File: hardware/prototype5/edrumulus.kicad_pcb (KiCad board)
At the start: 2 copper layers, 65 x 56.5 mm, 79 parts, among them J1 Trigger Connector, J2 Raspberry Pi GPIO pins, U1 ESP32-WROOM-32U, U2 AMS1117-3.3, U3 MCP1754S-3302xMB

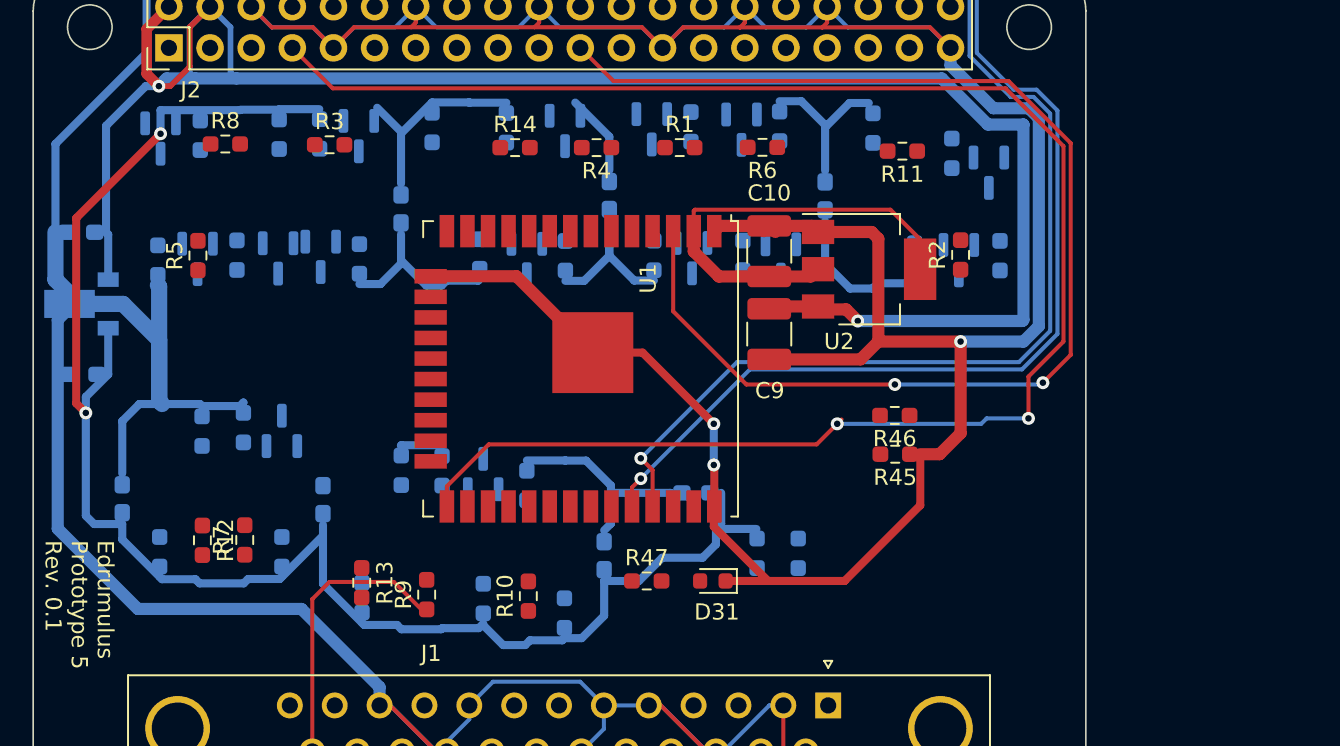
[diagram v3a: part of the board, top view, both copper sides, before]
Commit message: added the caps on the lower bias resistor for prototype 5
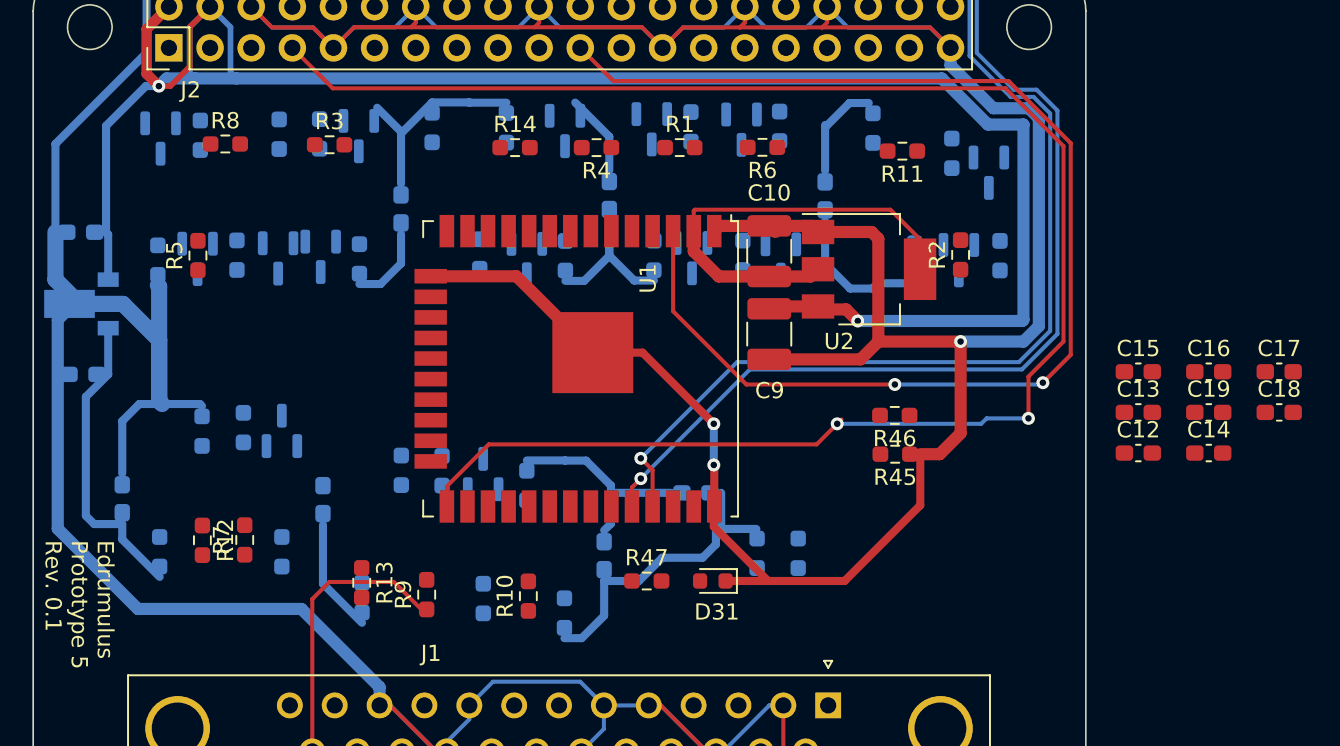
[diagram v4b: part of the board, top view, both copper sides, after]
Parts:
- added C12: 2n2, Capacitor_SMD:C_0603_1608Metric_Pad1.08x0.95mm_HandSolder, F.Cu at (174.8, 103.4)
- added C13: 2n2, Capacitor_SMD:C_0603_1608Metric_Pad1.08x0.95mm_HandSolder, F.Cu at (174.8, 100.9)
- added C14: 2n2, Capacitor_SMD:C_0603_1608Metric_Pad1.08x0.95mm_HandSolder, F.Cu at (179.2, 103.4)
- added C15: 2n2, Capacitor_SMD:C_0603_1608Metric_Pad1.08x0.95mm_HandSolder, F.Cu at (174.8, 98.4)
- added C16: 2n2, Capacitor_SMD:C_0603_1608Metric_Pad1.08x0.95mm_HandSolder, F.Cu at (179.2, 98.4)
- added C17: 2n2, Capacitor_SMD:C_0603_1608Metric_Pad1.08x0.95mm_HandSolder, F.Cu at (183.5, 98.4)
- added C18: 2n2, Capacitor_SMD:C_0603_1608Metric_Pad1.08x0.95mm_HandSolder, F.Cu at (183.5, 100.9)
- added C19: 2n2, Capacitor_SMD:C_0603_1608Metric_Pad1.08x0.95mm_HandSolder, F.Cu at (179.2, 100.9)
- C1, C2, C3, C4, C5, C6, C7: value 100 nF -> 100n
- C10, C9: value 22 µF -> 22µ
- C11, C8: value 1 µF -> 1µ
- R1, R12, R2, R3, R4, R5, R6, R7, R8, R9: value 100 kOhm -> 100k
- R10, R11, R13, R14: value 100 kOhm -> 22k
- R15, R16, R17, R18, R19, R20, R21, R22, R23, R24, R25, R26, R27, R28, R30, R32, R34, R38, R39, R40, R41, R42, R43, R44: value 22 kOhm -> 22k
- R29, R31, R35, R36: value 22 kOhm -> 100k
- R33, R37, R45, R46: value 10 kOhm -> 10k
- R47: value 470 Ohm -> 470
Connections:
- D12 pad 3: Net-(D12-Pad3) -> Net-(C17-Pad1)
- D13 pad 3: Net-(D13-Pad3) -> Net-(C18-Pad1)
- D3 pad 3: GPIO26 -> GPIO14
- D5 pad 3: GPIO14 -> GPIO26
- R10 pad 1: TOM1-RING -> GPIO14
- R10 pad 2: GPIO4 -> CRASH1-SLEEVE
- R11 pad 1: TOM1-TIP -> Net-(D4-Pad3)
- R11 pad 2: GPIO39 -> CRASH1-SLEEVE
- R13 pad 1: GPIO15 -> GPIO26
- R13 pad 2: TOM3-TIP -> CRASH1-SLEEVE
- R14 pad 1: GPIO33 -> Net-(D6-Pad3)
- R14 pad 2: KICK-TIP -> CRASH1-SLEEVE
- R17 pad 1: GPIO26 -> GPIO13
- R18 pad 1: Net-(D4-Pad3) -> Net-(D8-Pad3)
- R19 pad 1: GPIO14 -> Net-(D9-Pad3)
- R20 pad 1: Net-(D6-Pad3) -> 3V3
- R20 pad 2: CRASH1-SLEEVE -> GPIO14
- R21 pad 1: GPIO13 -> 3V3
- R21 pad 2: CRASH1-SLEEVE -> Net-(D4-Pad3)
- R22 pad 1: Net-(D8-Pad3) -> 3V3
- R22 pad 2: CRASH1-SLEEVE -> GPIO26
- R23 pad 1: Net-(D9-Pad3) -> 3V3
- R23 pad 2: CRASH1-SLEEVE -> Net-(D6-Pad3)
- R26 pad 2: GPIO26 -> GPIO13
- R27 pad 2: Net-(D4-Pad3) -> Net-(D8-Pad3)
- R28 pad 2: GPIO14 -> Net-(D9-Pad3)
- R29 pad 1: 3V3 -> GPIO15
- R29 pad 2: Net-(D6-Pad3) -> TOM3-TIP
- R3 pad 1: HI-HAT-RING -> CRASH1-RING
- R3 pad 2: GPIO26 -> GPIO14
- R30 pad 1: 3V3 -> Net-(C17-Pad1)
- R30 pad 2: GPIO13 -> CRASH1-SLEEVE
- R31 pad 1: 3V3 -> GPIO33
- R31 pad 2: Net-(D8-Pad3) -> KICK-TIP
- R32 pad 1: 3V3 -> Net-(C18-Pad1)
- R32 pad 2: Net-(D9-Pad3) -> CRASH1-SLEEVE
- R35 pad 1: Net-(D12-Pad3) -> TOM1-RING
- R35 pad 2: CRASH1-SLEEVE -> GPIO4
- R36 pad 1: Net-(D13-Pad3) -> TOM1-TIP
- R36 pad 2: CRASH1-SLEEVE -> GPIO39
- R39 pad 2: Net-(D12-Pad3) -> Net-(C17-Pad1)
- R4 pad 1: HI-HAT-TIP -> CRASH1-TIP
- R4 pad 2: GPIO32 -> GPIO34
- R40 pad 2: Net-(D13-Pad3) -> Net-(C18-Pad1)
- R5 pad 1: CRASH1-RING -> HI-HAT-RING
- R5 pad 2: GPIO14 -> GPIO26
- R6 pad 1: CRASH1-TIP -> HI-HAT-TIP
- R6 pad 2: GPIO34 -> GPIO32
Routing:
- net 3V3: track 128.3 -> 68.4 mm, vias 2 -> 0
- net CRASH1-SLEEVE: track 422.9 -> 412.0 mm

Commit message: delivery jstma for prototype 5 on 8/24/2022
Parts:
- added C20: 2n2, Capacitor_SMD:C_0603_1608Metric_Pad1.08x0.95mm_HandSolder, B.Cu at (127.8, 99.2)
- added C21: 2n2, Capacitor_SMD:C_0603_1608Metric_Pad1.08x0.95mm_HandSolder, B.Cu at (134.2, 99.2)
- added C22: 2n2, Capacitor_SMD:C_0603_1608Metric_Pad1.08x0.95mm_HandSolder, B.Cu at (131.0, 99.2)
- added C23: 2n2, Capacitor_SMD:C_0603_1608Metric_Pad1.08x0.95mm_HandSolder, B.Cu at (140.6, 99.2)
- added C24: 2n2, Capacitor_SMD:C_0603_1608Metric_Pad1.08x0.95mm_HandSolder, B.Cu at (143.6, 84.4)
- added C25: 2n2, Capacitor_SMD:C_0603_1608Metric_Pad1.08x0.95mm_HandSolder, B.Cu at (129.4, 99.2)
- C1, C11, C2, C3, C4, C5, C6, C7, C8, D10, R20, R21, R22, R23, R24, R25, R26, R27, R28, R31, R33, R37, R38, R39, R40, R43, R44, U3: moved to F.Cu
- C12, C13, C14, C15, C16, C17, C18, C19, R10, R11, R12, R13, R14, R45, R46, R7, R8, R9: moved to B.Cu
- moved D14 56.7 mm to (151.6, 126.8), turned to 90 degrees
- moved C18 47.7 mm to (135.8, 99.2), turned to 90 degrees
- moved R31 46.2 mm to (156.0, 114.8)
- moved D11 45.2 mm to (146.0, 126.8), turned to 90 degrees
- moved D12 44.4 mm to (138.0, 126.8), turned to 90 degrees
- moved R29 44.1 mm to (136.4, 124.2), turned to 90 degrees
- moved D15 43.9 mm to (157.2, 126.8), turned to 90 degrees
- moved D31 43.8 mm to (111.2, 88.4)
- moved C9 42.5 mm to (111.6, 83.0), turned to 90 degrees
- moved C13 42.2 mm to (132.6, 99.2), turned to 90 degrees
- moved C19 41.8 mm to (137.4, 99.2), turned to 90 degrees
- moved C17 41.8 mm to (143.6, 86.0), turned to 180 degrees
- moved U2 41.8 mm to (117.0, 85.0), turned to -90 degrees
- moved R8 41.3 mm to (126.6, 124.8), turned to -90 degrees
- moved R47 41.2 mm to (111.2, 87.0)
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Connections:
- net CRASH1-SLEEVE renamed GND
- C12 pad 1: GPIO14 -> GPIO36
- C16 pad 1: Net-(R34-Pad1) -> GPIO12
- C17 pad 1: Net-(C17-Pad1) -> GPIO15
- C18 pad 1: Net-(C18-Pad1) -> GPIO33
- C19 pad 1: GPIO4 -> GPIO25
- D10 pad 3: Net-(D10-Pad3) -> HI-HAT-CONTROL-TIP
- D11 pad 3: Net-(R34-Pad1) -> GPIO12
- D12 pad 3: Net-(C17-Pad1) -> GPIO15
- D13 pad 3: Net-(C18-Pad1) -> GPIO33
- D14 pad 3: GPIO4 -> GPIO25
- D15 pad 3: Net-(D15-Pad3) -> GPIO39
- D2 pad 3: Net-(R16-Pad1) -> GPIO14
- D3 pad 3: GPIO14 -> GPIO36
- D4 pad 3: Net-(D4-Pad3) -> GPIO34
- D6 pad 3: Net-(D6-Pad3) -> GPIO32
- D8 pad 3: Net-(D8-Pad3) -> GPIO27
- D9 pad 3: Net-(D9-Pad3) -> GPIO2
- R10 pad 1: GPIO14 -> GPIO36
- R11 pad 1: Net-(D4-Pad3) -> GPIO34
- R14 pad 1: Net-(D6-Pad3) -> GPIO32
- R16 pad 1: Net-(R16-Pad1) -> GPIO14
- R18 pad 1: Net-(D8-Pad3) -> GPIO27
- R19 pad 1: Net-(D9-Pad3) -> GPIO2
- R2 pad 2: GPIO36 -> GPIO14
- R20 pad 2: GPIO14 -> GPIO36
- R21 pad 2: Net-(D4-Pad3) -> GPIO34
- R23 pad 2: Net-(D6-Pad3) -> GPIO32
- R25 pad 2: Net-(R16-Pad1) -> GPIO14
- R27 pad 2: Net-(D8-Pad3) -> GPIO27
- R28 pad 2: Net-(D9-Pad3) -> GPIO2
- R3 pad 2: GPIO14 -> GPIO36
- R30 pad 1: Net-(C17-Pad1) -> GPIO15
- R32 pad 1: Net-(C18-Pad1) -> GPIO33
- R33 pad 1: GPIO25 -> GPIO4
- R34 pad 1: Net-(R34-Pad1) -> GPIO12
- R35 pad 2: GPIO4 -> GPIO25
- R37 pad 2: Net-(D10-Pad3) -> HI-HAT-CONTROL-TIP
- R38 pad 2: Net-(R34-Pad1) -> GPIO12
- R39 pad 2: Net-(C17-Pad1) -> GPIO15
- R40 pad 2: Net-(C18-Pad1) -> GPIO33
- R41 pad 1: GPIO4 -> GPIO25
- R42 pad 1: Net-(D15-Pad3) -> GPIO39
- R43 pad 2: GPIO4 -> GPIO25
- R44 pad 2: Net-(D15-Pad3) -> GPIO39
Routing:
- net GND: track 412.0 -> 0.00 mm, vias 3 -> 0
- net RASPI-VIN: track 119.7 -> 0.00 mm, vias 2 -> 0
- net PI-GPIO4: track 107.1 -> 0.00 mm, vias 2 -> 0
- net ESP-UART0-RX: track 99.3 -> 0.00 mm, vias 1 -> 0
- net ESP-UART0-TX: track 96.1 -> 0.00 mm, vias 1 -> 0
- net PI-GPIO9: track 77.9 -> 0.00 mm, vias 2 -> 0
- net 3V3: track 68.4 -> 0.00 mm
- net ESP32-3V3: track 27.6 -> 0.00 mm
- net GPIO36: track 0.00 -> 19.7 mm, vias 0 -> 2
- net RIDE-BELL-TIP: track 17.7 -> 0.00 mm
- net CRASH1-RING: track 0.00 -> 3.28 mm
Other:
- copper layers 2 -> 4

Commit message: Add 3 0603 capacitors to the ESP32_3V3 net. Add one 1210 ferrite bead between RASPI-VIN and pin1 of U3. Add one 1210 ferrite bead between RASPI-VIN and pin3 of U2. Also place an 0603 cap on the RASPI-VIN side of each ferrite.
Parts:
- added C26: 1µ, Capacitor_SMD:C_0603_1608Metric_Pad1.08x0.95mm_HandSolder, F.Cu at (185.9, 97.4)
- added C27: 22µ, Capacitor_SMD:C_0603_1608Metric_Pad1.08x0.95mm_HandSolder, F.Cu at (181.5, 99.9)
- added C28: 1µ, Capacitor_SMD:C_0603_1608Metric_Pad1.08x0.95mm_HandSolder, F.Cu at (181.5, 97.4)
- added C29: 100n, Capacitor_SMD:C_0603_1608Metric_Pad1.08x0.95mm_HandSolder, F.Cu at (181.5, 94.9)
- added C30: 10n, Capacitor_SMD:C_0603_1608Metric_Pad1.08x0.95mm_HandSolder, F.Cu at (185.9, 94.9)
- added FB1: FerriteBead, Inductor_SMD:L_1210_3225Metric_Pad1.42x2.65mm_HandSolder, F.Cu at (176.4, 100.0)
- added FB2: FerriteBead, Inductor_SMD:L_1210_3225Metric_Pad1.42x2.65mm_HandSolder, F.Cu at (176.4, 95.7)
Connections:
- C8 pad 1: RASPI-VIN -> Net-(C8-Pad1)
- C9 pad 1: RASPI-VIN -> Net-(C9-Pad1)
- U2 pad 3: RASPI-VIN -> Net-(C9-Pad1)
- U3 pad 1: RASPI-VIN -> Net-(C8-Pad1)
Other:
- board text added: "Edrumulus Prototype 5 Rev. 0.2"
- board text removed: "Edrumulus Prototype 5 Rev. 0.1"

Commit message: delivery jstma for prototype 5 on 8/28/2022
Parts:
- added MH1: MountingHole_2.7mm_M2.5, MountingHole:MountingHole_2.7mm_M2.5, F.Cu at (172.9, 125.7)
- added MH2: MountingHole_2.7mm_M2.5, MountingHole:MountingHole_2.7mm_M2.5, F.Cu at (230.9, 125.7)
- added MH3: MountingHole_2.7mm_M2.5, MountingHole:MountingHole_2.7mm_M2.5, F.Cu at (172.9, 174.7)
- added MH4: MountingHole_2.7mm_M2.5, MountingHole:MountingHole_2.7mm_M2.5, F.Cu at (230.9, 174.7)
- C11, C26, C27, C29, C30, C8, FB1, R1, R6, U3: moved to B.Cu
- J2: footprint Connector_PinHeader_2.54mm:PinHeader_2x20_P2.54mm_Vertical -> Connector_PinSocket_2.54mm:PinSocket_2x20_P2.54mm_Vertical; moved to B.Cu
- R12, R9: moved to F.Cu
- moved D31 129.7 mm to (233.4, 131.8), turned to -90 degrees
- moved R47 128.5 mm to (231.6, 131.8), turned to -90 degrees
- moved R9 105.9 mm to (220.0, 163.3)
- moved D9 105.9 mm to (220.0, 163.3)
- moved R3 100.2 mm to (210.1, 163.3)
- moved D3 100.2 mm to (210.1, 163.3)
- moved R8 96.8 mm to (210.6, 172.8)
- moved D7 96.6 mm to (214.8, 175.5)
- moved R7 95.7 mm to (212.2, 172.8)
- moved D8 95.6 mm to (208.0, 175.5)
- moved D12 95.3 mm to (220.0, 175.5)
- moved R29 94.5 mm to (217.4, 172.9)
- moved C10 93.0 mm to (185.4, 151.4)
- moved C9 91.6 mm to (180.6, 143.3), turned to 0 degrees
- moved U2 90.1 mm to (179.6, 149.8)
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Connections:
- C12 pad 1: GPIO36 -> GPIO14
- C20 pad 1: GPIO14 -> GPIO36
- D2 pad 3: GPIO14 -> GPIO36
- D3 pad 3: GPIO36 -> GPIO14
- J1 pad 0: (no net) -> unconnected-(J1-Pad0)
- R1 pad 1: SNARE-RING -> RIDE-TIP
- R10 pad 1: GPIO36 -> GPIO14
- R12 pad 2: TOM2-TIP -> SNARE-TIP
- R16 pad 1: GPIO14 -> GPIO36
- R2 pad 1: SNARE-TIP -> CRASH1-RING
- R2 pad 2: GPIO14 -> GPIO36
- R20 pad 2: GPIO36 -> GPIO14
- R25 pad 2: GPIO14 -> GPIO36
- R29 pad 2: TOM3-TIP -> TOM1-TIP
- R3 pad 1: CRASH1-RING -> SNARE-RING
- R3 pad 2: GPIO36 -> GPIO14
- R31 pad 2: KICK-TIP -> HI-HAT-RING
- R35 pad 1: TOM1-RING -> TOM3-TIP
- R36 pad 1: TOM1-TIP -> RIDE-BELL-TIP
- R5 pad 1: HI-HAT-RING -> HI-HAT-TIP
- R6 pad 1: HI-HAT-TIP -> RIDE-RING
- R7 pad 1: RIDE-RING -> TOM1-RING
- R8 pad 1: RIDE-TIP -> TOM2-TIP
- R9 pad 1: RIDE-BELL-TIP -> KICK-TIP
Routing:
- net HI-HAT-CONTROL-TIP: track 0.00 -> 94.4 mm, vias 0 -> 1
- net GPIO15: track 0.00 -> 53.4 mm, vias 0 -> 2
- net GPIO13: track 0.00 -> 42.3 mm, vias 0 -> 2
- net GPIO2: track 0.00 -> 41.9 mm, vias 0 -> 2
- net PI-GPIO9: track 0.00 -> 39.2 mm, vias 0 -> 2
- net GPIO32: track 0.00 -> 37.3 mm, vias 0 -> 2
- net GPIO35: track 0.00 -> 35.9 mm, vias 0 -> 2
- net GPIO27: track 0.00 -> 33.9 mm, vias 0 -> 2
- net Net-(R47-Pad1): track 0.00 -> 33.9 mm, vias 0 -> 2
- net GPIO25: track 0.00 -> 33.6 mm, vias 0 -> 2
- net GPIO39: track 0.00 -> 32.7 mm, vias 0 -> 2
- net PI-GPIO4: track 0.00 -> 28.5 mm, vias 0 -> 1
- net GPIO12: track 0.00 -> 21.8 mm, vias 0 -> 2
- net GPIO34: track 0.00 -> 20.9 mm, vias 0 -> 2
- net GPIO14: track 0.00 -> 20.8 mm, vias 0 -> 2
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- added copper zone on B.Cu, net 3V3
- added copper zone on F.Cu, net 3V3
- added copper zone on In2.Cu, net 3V3
- added copper zone on B.Cu, net ESP32-3V3
- added copper zone on F.Cu, net ESP32-3V3
- added copper zone on B.Cu, net GND
- added copper zone on F.Cu, net GND
- added copper zone on In1.Cu, net GND
- added copper zone on B.Cu, net Net-(C8-Pad1)
- added copper zone on F.Cu, net Net-(C9-Pad1)
- added copper zone on B.Cu, net RASPI-VIN
- added copper zone on F.Cu, net RASPI-VIN
- added copper zone on In1.Cu, net RASPI-VIN
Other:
- board size 65 x 56.5 mm -> 65 x 56 mm
- board text added: "J2 comes with pi hat mounting template. All parts placed with reference to pin1 of J2."
- board text added: "TODO: Vias under esp32 gnd pad must be untented. Vias in the pad of FB1 must be untented too. Meanwhile the rest of the vias must be tented. pin 15 is not connected to ground. I don't think it needs to be, but if there is a problem it might be good to be able to ground that pin. I guess a wire can be added to the ground side of C6. Maybe beef up the wires from the db25 into the 100k resistor."

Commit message: delivery jstma for prototype 5 on 8/28/2022 #2
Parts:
- added C31: 100n, Capacitor_SMD:C_0603_1608Metric_Pad1.08x0.95mm_HandSolder, F.Cu at (180.7, 156.0)
- added C32: 100n, Capacitor_SMD:C_0603_1608Metric_Pad1.08x0.95mm_HandSolder, F.Cu at (180.7, 163.6)
- added C33: 100n, Capacitor_SMD:C_0603_1608Metric_Pad1.08x0.95mm_HandSolder, B.Cu at (180.3, 176.8)
- added C34: 100n, Capacitor_SMD:C_0603_1608Metric_Pad1.08x0.95mm_HandSolder, B.Cu at (223.5, 176.8)
- added C35: 100n, Capacitor_SMD:C_0603_1608Metric_Pad1.08x0.95mm_HandSolder, F.Cu at (223.5, 163.6)
- added C36: 100n, Capacitor_SMD:C_0603_1608Metric_Pad1.08x0.95mm_HandSolder, F.Cu at (223.5, 156.0)
- added C37: 100n, Capacitor_SMD:C_0603_1608Metric_Pad1.08x0.95mm_HandSolder, F.Cu at (223.5, 144.8)
- added C38: 100n, Capacitor_SMD:C_0603_1608Metric_Pad1.08x0.95mm_HandSolder, F.Cu at (223.5, 131.3)
- D10: moved to B.Cu
- moved D10 1.15 mm to (193.5, 164.2)
- moved D31 0.40 mm to (233.4, 131.4)
- moved R47 0.40 mm to (231.7, 131.4)
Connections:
- R31 pad 2: HI-HAT-RING -> HI-HAT-TIP
- R35 pad 1: TOM3-TIP -> RIDE-RING
- R5 pad 1: HI-HAT-TIP -> HI-HAT-RING
- R6 pad 1: RIDE-RING -> TOM3-TIP
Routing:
- net TOM3-TIP: track 3.19 -> 11.5 mm, vias 0 -> 1
- net RIDE-RING: track 1.62 -> 9.07 mm
- net HI-HAT-RING: track 3.16 -> 9.32 mm, vias 0 -> 1
- net GND: track 18.7 -> 14.7 mm, vias 44 -> 122
- net 3V3: track 15.2 -> 19.1 mm, vias 31 -> 34
- net HI-HAT-CONTROL-TIP: track 94.4 -> 92.2 mm
- net HI-HAT-TIP: track 3.48 -> 4.77 mm, vias 0 -> 1
- net GPIO15: track 53.4 -> 54.2 mm
- net GPIO2: track 41.9 -> 42.4 mm
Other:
- board text added: "Pin 15 of esp32 is not connected to ground. It's a DRC error, but I can't mark the pin as not connected in the schematic. I don't think it needs to be, but if there is a problem it might be good to be able to ground that pin. In that case, a wire can be added from pin 15 to the ground side of C6."
- board text removed: "TODO: Vias under esp32 gnd pad must be untented. Vias in the pad of FB1 must be untented too. Meanwhile the rest of the vias must be tented. pin 15 is not connected to ground. I don't think it needs to be, but if there is a problem it might be good to be able to ground that pin. I guess a wire can be added to the ground side of C6. Maybe beef up the wires from the db25 into the 100k resistor."
